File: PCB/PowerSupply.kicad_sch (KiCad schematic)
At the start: 34 parts, among them U1 TPS54325_PWP_14, U2 TPS54294PWP

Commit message: dump
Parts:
- L2: value 1.5u -> 1.5uH
- L3: value 2.2u -> 2.2uH
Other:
- note added: "4.5V - 18V"
- moved on the sheet: C1, C10, C11, C12, C13, C14, C15, C16, C17, C18, C19, C2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

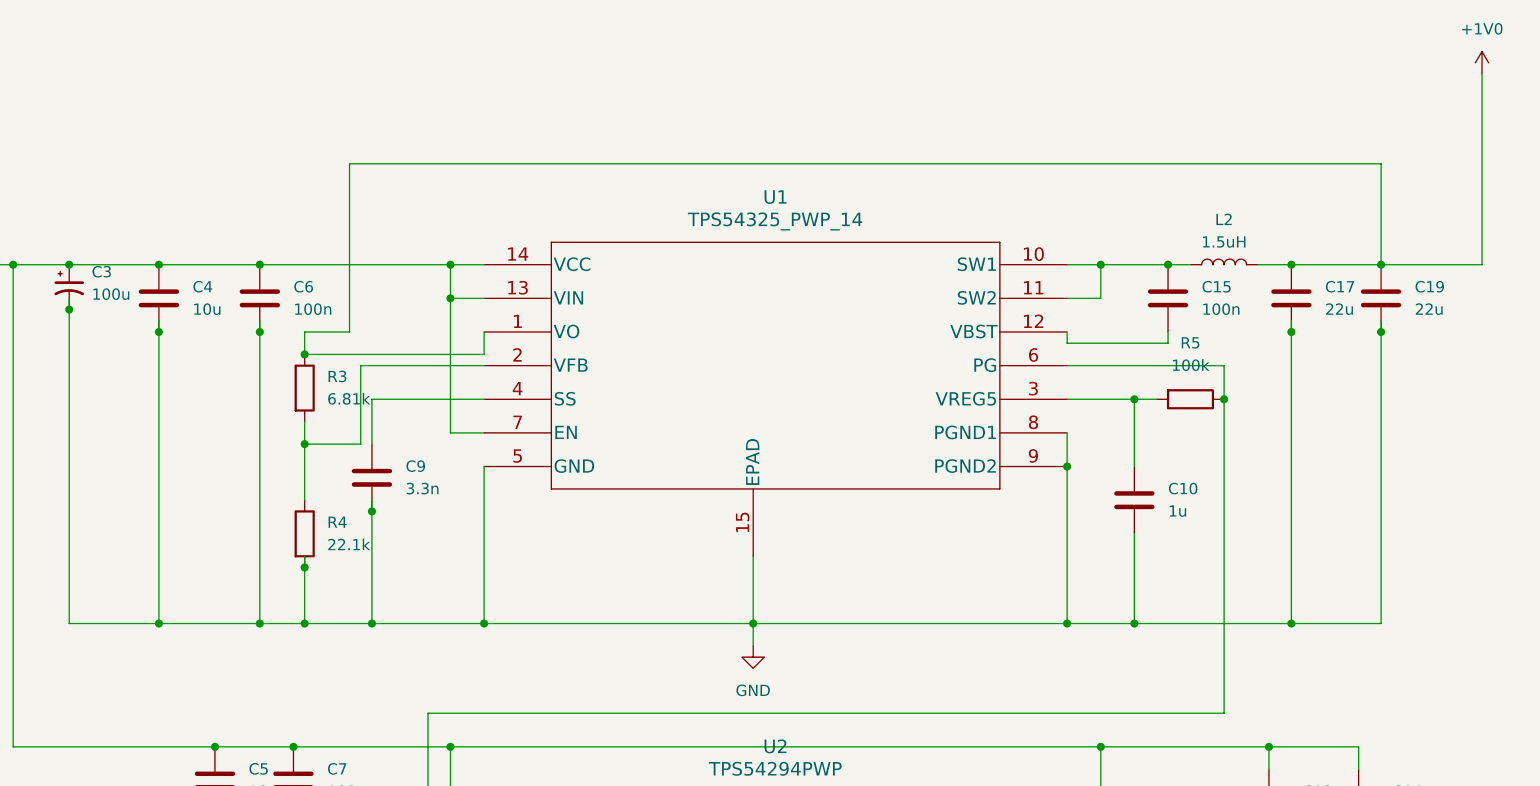
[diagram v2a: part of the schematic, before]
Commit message: 1.5V added
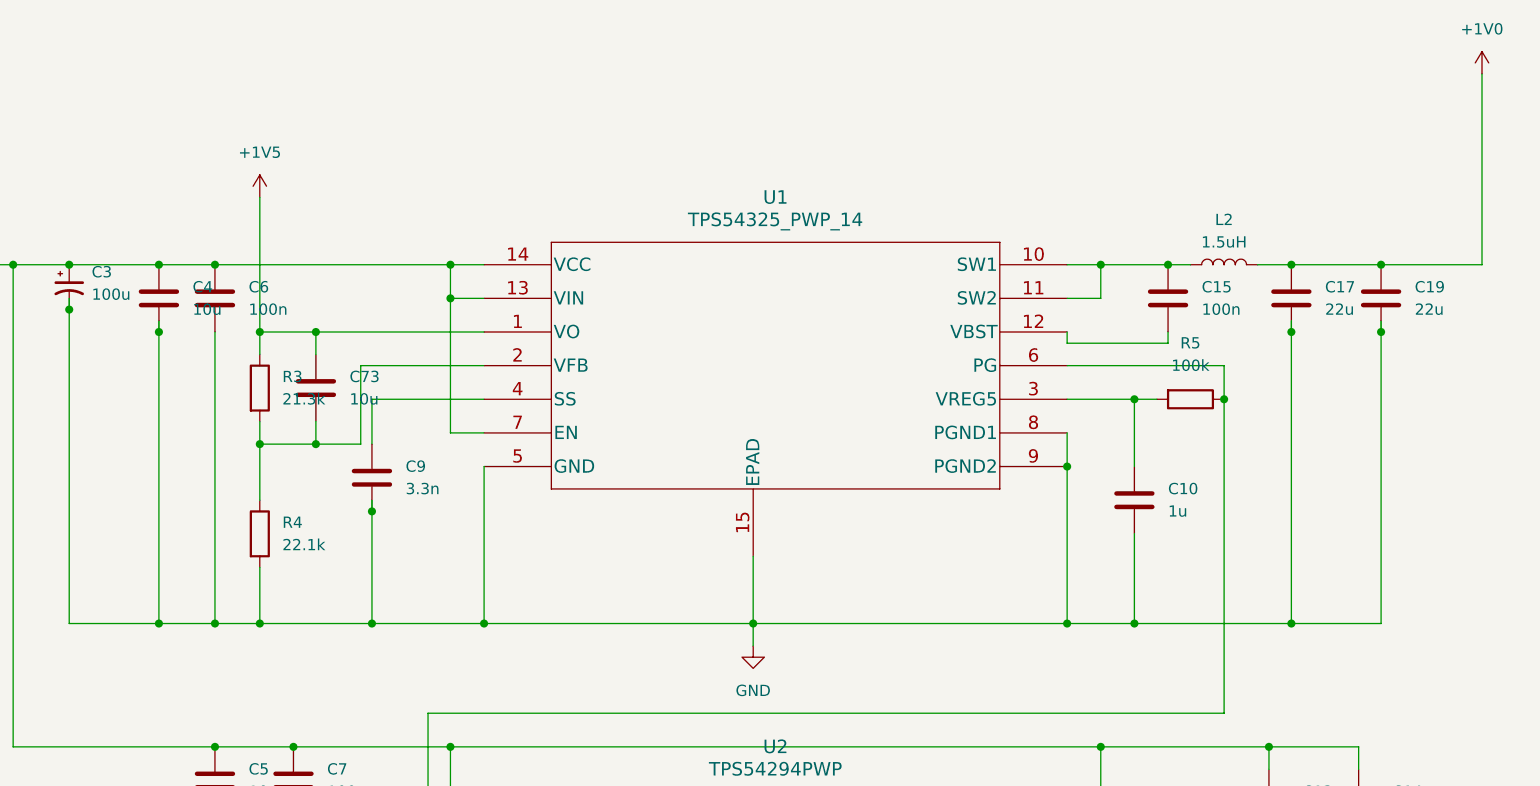
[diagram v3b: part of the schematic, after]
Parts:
- added C73: 10u, symbol Device:C
- R3: value 6.81k -> 21.3k
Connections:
- net +1V0: no longer R3.1, U1.1 (VO)
- net at R3.2, R4.1, U1.2 (VFB): now also C73.2
- new net +1V5: C73.1, R3.1, U1.1 (VO)
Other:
- moved on the sheet: C6, R3, R4

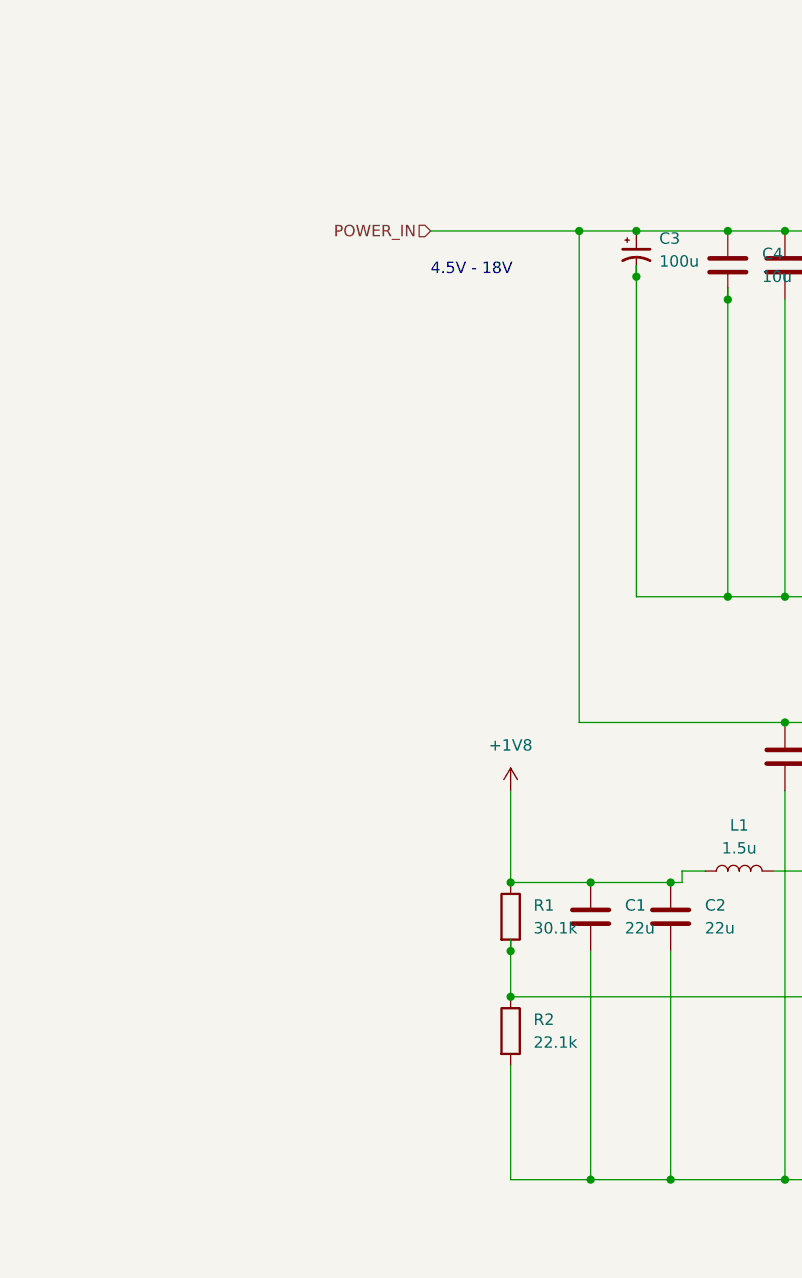
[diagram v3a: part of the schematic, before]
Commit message: add barrel jack
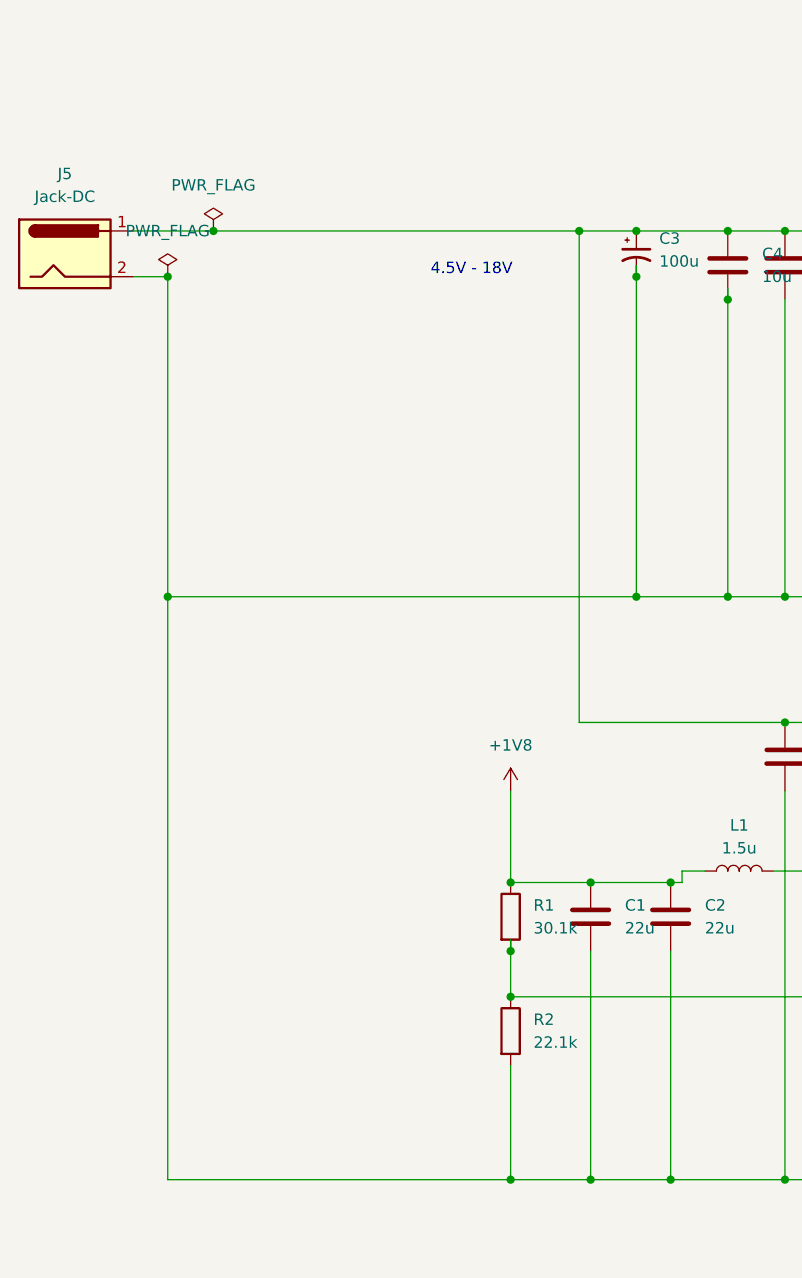
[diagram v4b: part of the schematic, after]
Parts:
- added J5: Jack-DC, symbol Connector:Jack-DC
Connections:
- net GND: now also J5.2
- net POWER_IN: no longer names the net of C13.1, C14.1, C3.1, C4.1, C5.1, C6.1, C7.1, U1.13 (VIN), U1.14 (VCC), U1.7 (EN), U2.1 (VIN1), U2.16 (VIN2)
- net POWER_IN: now also J5.1
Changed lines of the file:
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@@
   (junction (at 146.05 140.97) (diameter 0) (color 0 0 0 0)
   )
+  (junction (at 120.65 127) (diameter 0) (color 0 0 0 0)
+  )
   (junction (at 130.81 93.98) (diameter 0) (color 0 0 0 0)
   )
@@
   (junction (at 294.64 191.77) (diameter 0) (color 0 0 0 0)
   )
+  (junction (at 106.68 191.77) (diameter 0) (color 0 0 0 0)
+  )
   (junction (at 106.68 166.37) (diameter 0) (color 0 0 0 0)
   )
@@
   (junction (at 153.67 158.75) (diameter 0) (color 0 0 0 0)
   )
+  (junction (at 68.58 127) (diameter 0) (color 0 0 0 0)
+  )
   (junction (at 115.57 191.77) (diameter 0) (color 0 0 0 0)
   )
   (junction (at 124.46 191.77) (diameter 0) (color 0 0 0 0)
   )
+  (junction (at 73.66 86.36) (diameter 0) (color 0 0 0 0)
+  )
   (junction (at 242.57 171.45) (diameter 0) (color 0 0 0 0)
   )
@@
   )
   (junction (at 130.81 127) (diameter 0) (color 0 0 0 0)
+  )
+  (junction (at 68.58 91.44) (diameter 0) (color 0 0 0 0)
   )
   (junction (at 198.12 127) (diameter 0) (color 0 0 0 0)
@@
     (stroke (width 0) (type default))
   )
-  (wire (pts (xy 97.79 86.36) (xy 114.3 86.36))
+  (wire (pts (xy 64.77 86.36) (xy 73.66 86.36))
     (stroke (width 0) (type default))
   )
@@
     (stroke (width 0) (type default))
   )
+  (wire (pts (xy 68.58 127) (xy 120.65 127))
+    (stroke (width 0) (type default))
+  )
   (wire (pts (xy 259.08 127) (xy 269.24 127))
     (stroke (width 0) (type default))
   )
+  (wire (pts (xy 73.66 86.36) (xy 114.3 86.36))
+    (stroke (width 0) (type default))
+  )
   (wire (pts (xy 167.64 109.22) (xy 167.64 127))
     (stroke (width 0) (type default))
@@
     (stroke (width 0) (type default))
   )
+  (wire (pts (xy 64.77 91.44) (xy 68.58 91.44))
+    (stroke (width 0) (type default))
+  )
   (wire (pts (xy 337.82 158.75) (xy 347.98 158.75))
     (stroke (width 0) (type default))
@@
     (stroke (width 0) (type default))
   )
+  (wire (pts (xy 68.58 127) (xy 68.58 191.77))
+    (stroke (width 0) (type default))
+  )
   (wire (pts (xy 233.68 168.91) (xy 306.07 168.91))
     (stroke (width 0) (type default))
@@
     (stroke (width 0) (type default))
   )
+  (wire (pts (xy 68.58 191.77) (xy 106.68 191.77))
+    (stroke (width 0) (type default))
+  )
   (wire (pts (xy 306.07 167.64) (xy 306.07 168.91))
     (stroke (width 0) (type default))
@@
   )
   (wire (pts (xy 236.22 191.77) (xy 196.85 191.77))
+    (stroke (width 0) (type default))
+  )
+  (wire (pts (xy 68.58 91.44) (xy 68.58 127))
     (stroke (width 0) (type default))
   )
@@
   (text "4.5V - 18V" (at 97.79 91.44 0)
     (effects (font (size 1.27 1.27)) (justify left bottom))
-  )
-  (hierarchical_label "POWER_IN" (shape input) (at 97.79 86.36 180) (fields_autoplaced)
-    (effects (font (size 1.27 1.27)) (justify right))
   )
   (symbol (lib_id "Device:R") (at 142.24 100.33 0) (unit 1)
@@
     )
   )
+  (symbol (lib_id "Connector:Jack-DC") (at 57.15 88.9 0) (unit 1)
+    (in_bom yes) (on_board yes) (dnp no) (fields_autoplaced)
+    (property "Reference" "J5" (at 57.15 80.01 0)
+      (effects (font (size 1.27 1.27)))
+    )
+    (property "Value" "Jack-DC" (at 57.15 82.55 0)
+      (effects (font (size 1.27 1.27)))
+    )
+    (property "Footprint" "" (at 58.42 89.916 0)
+      (effects (font (size 1.27 1.27)) hide)
+    )
+    (property "Datasheet" "~" (at 58.42 89.916 0)
+      (effects (font (size 1.27 1.27)) hide)
+    )
+    (pin "1")
+    (pin "2")
+    (instances
+      (project "RayTracingPCB"
+        (path "/e9047d94-28be-4266-894b-6ee25ef088bd/30b429a8-b068-46fd-8deb-ee4af8cda04e"
+          (reference "J5") (unit 1)
+        )
+      )
+    )
+  )
   (symbol (lib_id "Device:R") (at 306.07 177.8 0) (unit 1)
     (in_bom yes) (on_board yes) (dnp no) (fields_autoplaced)
@@
         (path "/e9047d94-28be-4266-894b-6ee25ef088bd/30b429a8-b068-46fd-8deb-ee4af8cda04e"
           (reference "C12") (unit 1)
+        )
+      )
+    )
+  )
+  (symbol (lib_id "power:PWR_FLAG") (at 68.58 91.44 0) (unit 1)
+    (in_bom yes) (on_board yes) (dnp no) (fields_autoplaced)
+    (property "Reference" "#FLG02" (at 68.58 89.535 0)
+      (effects (font (size 1.27 1.27)) hide)
+    )
+    (property "Value" "PWR_FLAG" (at 68.58 86.36 0)
+      (effects (font (size 1.27 1.27)))
+    )
+    (property "Footprint" "" (at 68.58 91.44 0)
+      (effects (font (size 1.27 1.27)) hide)
+    )
+    (property "Datasheet" "~" (at 68.58 91.44 0)
+      (effects (font (size 1.27 1.27)) hide)
+    )
+    (pin "1")
+    (instances
+      (project "RayTracingPCB"
+        (path "/e9047d94-28be-4266-894b-6ee25ef088bd/30b429a8-b068-46fd-8deb-ee4af8cda04e"
+          (reference "#FLG02") (unit 1)
         )
       )
@@
         )
       )
+    )
+  )
+  (symbol (lib_id "power:PWR_FLAG") (at 73.66 86.36 0) (unit 1)
+    (in_bom yes) (on_board yes) (dnp no) (fields_autoplaced)
+    (property "Reference" "#FLG01" (at 73.66 84.455 0)
+      (effects (font (size 1.27 1.27)) hide)
+    )
+    (property "Value" "PWR_FLAG" (at 73.66 81.28 0)
+      (effects (font (size 1.27 1.27)))
+    )
+    (property "Footprint" "" (at 73.66 86.36 0)
+      (effects (font (size 1.27 1.27)) hide)
+    )
+    (property "Datasheet" "~" (at 73.66 86.36 0)
+      (effects (font (size 1.27 1.27)) hide)
+    )
+    (pin "1")
+    (instances
+      (project "RayTracingPCB"
+        (path "/e9047d94-28be-4266-894b-6ee25ef088bd/30b429a8-b068-46fd-8deb-ee4af8cda04e"
+          (reference "#FLG01") (unit 1)
+        )
+      )

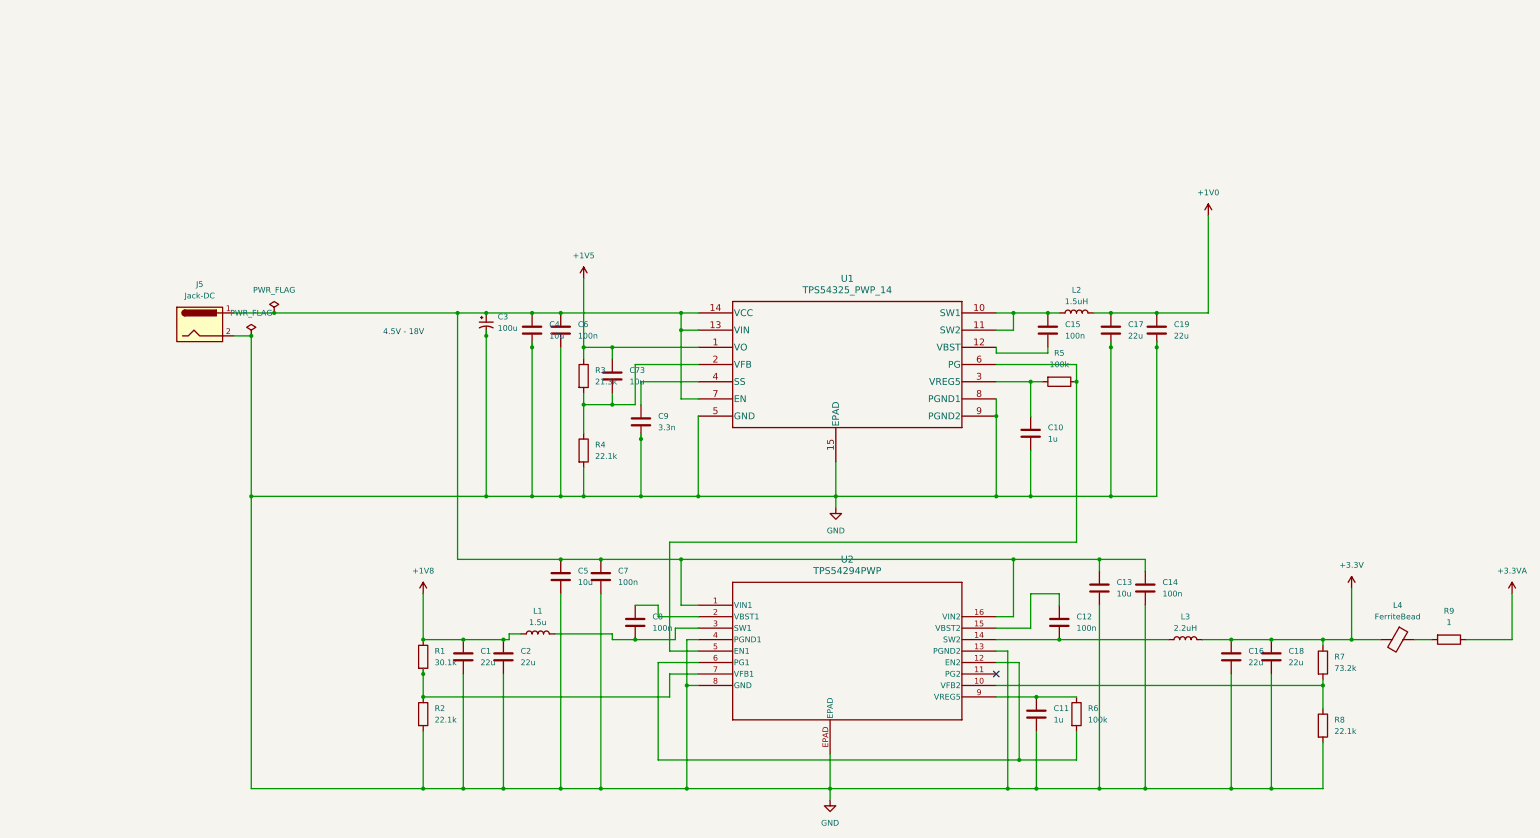
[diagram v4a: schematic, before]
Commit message: add usb micro and switches
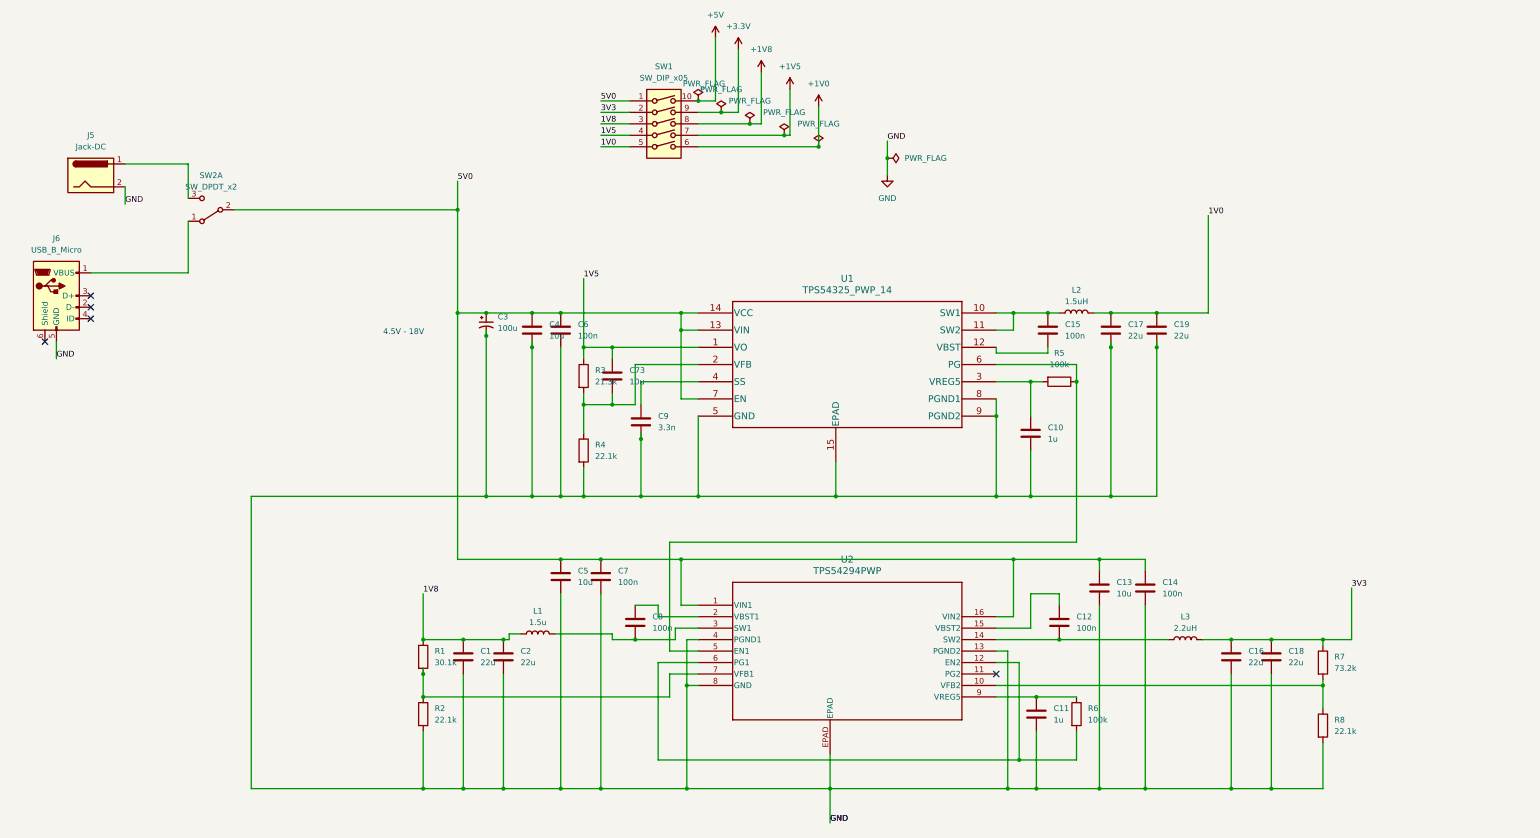
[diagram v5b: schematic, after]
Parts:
- removed L4: FerriteBead, symbol Device:FerriteBead
- removed R9: 1, symbol Device:R
- added J6: USB_B_Micro, symbol Connector:USB_B_Micro
- added SW1: SW_DIP_x05, symbol Switch:SW_DIP_x05
- added SW2: SW_DPDT_x2, symbol Switch:SW_DPDT_x2
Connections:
- net +1V0: now also SW1.6; no longer C17.1, C19.1, L2.2
- net +1V5: now also SW1.7; no longer C73.1, R3.1, U1.1 (VO)
- net +1V8: now also SW1.8; no longer C1.1, C2.1, L1.1, R1.1
- net +3.3V: now also SW1.9; no longer C16.1, C18.1, L3.2, R7.1
- net GND: now also J6.5 (GND)
- net 5V0: now reaches C13.1, C14.1, C3.1, C4.1, C5.1, C6.1, C7.1, U1.13 (VIN), U1.14 (VCC), U1.7 (EN), U2.1 (VIN1), U2.16 (VIN2)
- net 5V0: now also SW1.1, SW2.2 (B); no longer J5.1
- new net: J5.1, SW2.3 (C)
- new net: J6.1 (VBUS), SW2.1 (A)
- new net +5V: SW1.10
- new net 1V0: C17.1, C19.1, L2.2, SW1.5
- new net 1V5: C73.1, R3.1, SW1.4, U1.1 (VO)
- new net 1V8: C1.1, C2.1, L1.1, R1.1, SW1.3
- new net 3V3: C16.1, C18.1, L3.2, R7.1, SW1.2
- no-connect marks 1 -> 5
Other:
- moved on the sheet: J5
